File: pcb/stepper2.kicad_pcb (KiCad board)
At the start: 2 copper layers, 92 x 138 mm, 58 parts, among them J1 DA15_Receptacle_MountingHoles, J10 Conn_01x07_Pin, J11 FAN, J12 Conn_01x03_Pin, J13 Conn_01x03_Pin, J14 Conn_01x03_Pin, J2 DA15_Receptacle_MountingHoles, J3 DA15_Receptacle_MountingHoles, J4 DE15_Receptacle_HighDensity, J5 DE15_Receptacle_HighDensity, J6 DE15_Receptacle_HighDensity, J7 Conn_01x04_Pin, J8 Conn_01x05_Pin, J9 Conn_01x06_Pin, SW1 SW_Push, SW2 SW_Push, SW3 SW_Push, SW4 SW_Push, SW5 SW_Push, SW6 SW_Push, U1 AM26LS32ACN, U2 AM26LS32Ax, U3 AM26LS32ACN, U4 TMC2209_BIGTREETECH, U5 TMC2209_BIGTREETECH, U6 TMC2209_BIGTREETECH

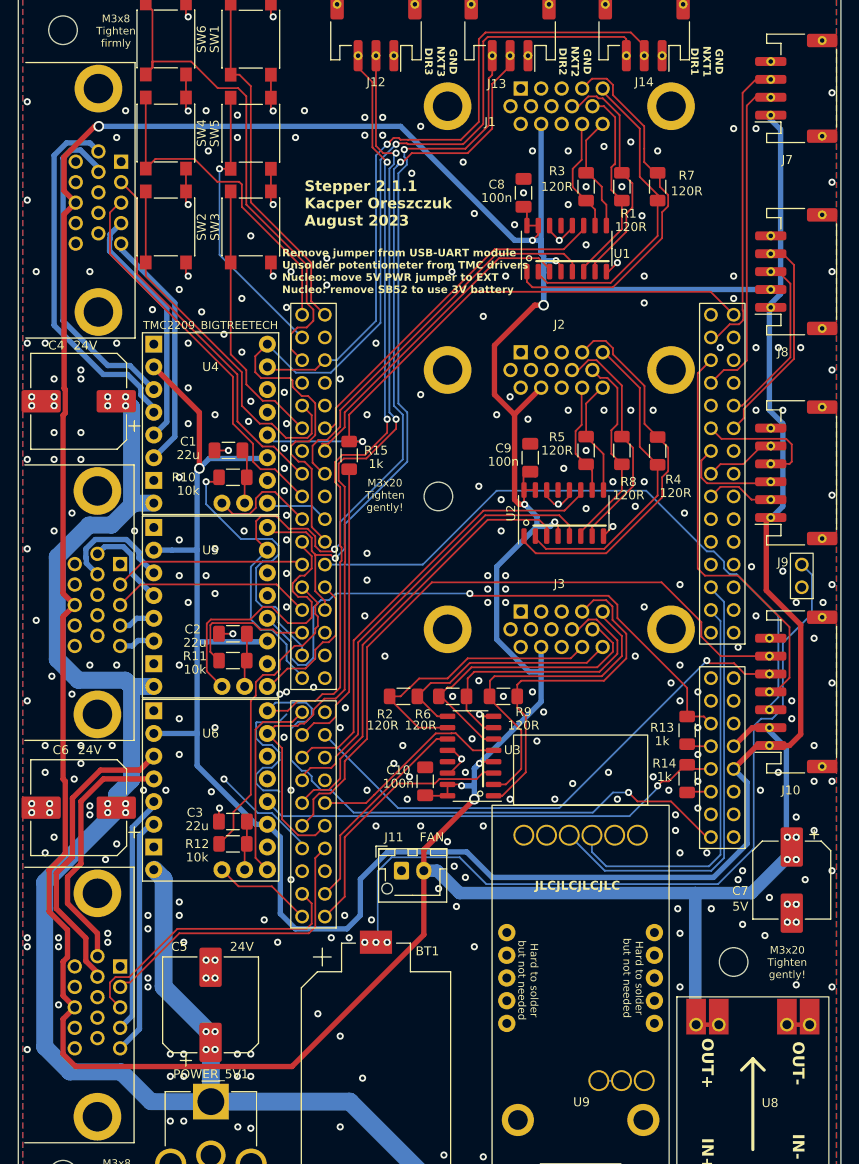
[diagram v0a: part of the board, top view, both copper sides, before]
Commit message: fixed flipped rotation direction relative to stepper 1
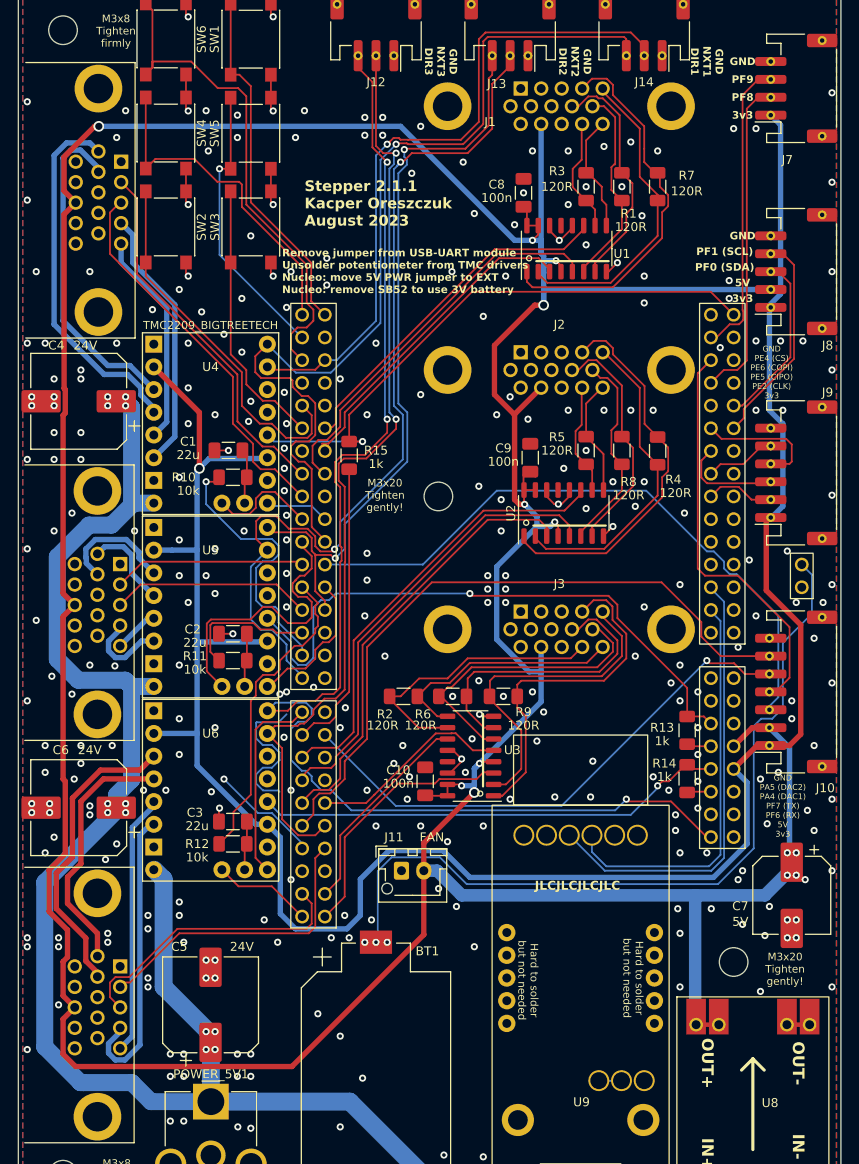
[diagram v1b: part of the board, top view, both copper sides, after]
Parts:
- moved C7 1.70 mm to (86.5, 101.8)
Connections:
- J4 pad 4: MYA1 -> MYB1
- J4 pad 5: MYB1 -> MYA1
- J5 pad 4: MYA2 -> MYB2
- J5 pad 5: MYB2 -> MYA2
- J6 pad 4: MYA3 -> MYB3
- J6 pad 5: MYB3 -> MYA3
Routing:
- net MYB3: track 26.8 -> 33.4 mm
- net MYB2: track 3.96 -> 9.51 mm
- net +5V: track 467.5 -> 472.3 mm
- net MYA1: track 27.5 -> 24.1 mm
- net MYB1: track 27.4 -> 29.7 mm
- net MYA3: track 26.9 -> 29.2 mm
- net MYA2: track 4.10 -> 5.04 mm
- net DIR3: track 151.2 -> 150.4 mm
- net GND: vias 333 -> 330
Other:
- board text added: "3v3"
- board text added: "5V"
- board text added: "GND"
- board text added: "GND PA5 (DAC2) PA4 (DAC1) PF7 (TX) PF6 (RX) 5V 3v3"
- board text added: "GND PE4 (CS) PE6 (COPI) PE5 (CIPO) PE2 (CLK) 3v3"
- board text added: "PF0 (SDA)"
- board text added: "PF1 (SCL)"
- board text added: "PF8"
- board text added: "PF9"

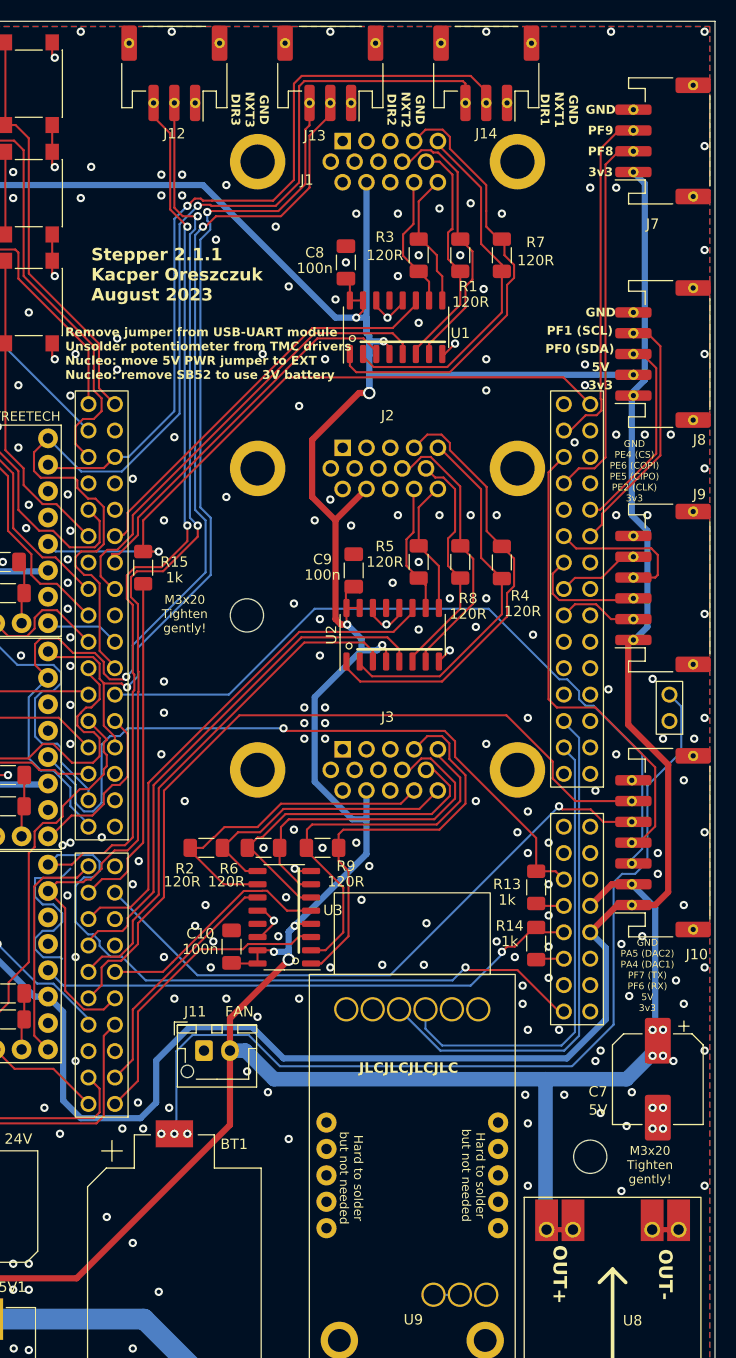
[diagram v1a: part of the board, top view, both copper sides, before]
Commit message: Added voltage shifter between FTDI and board
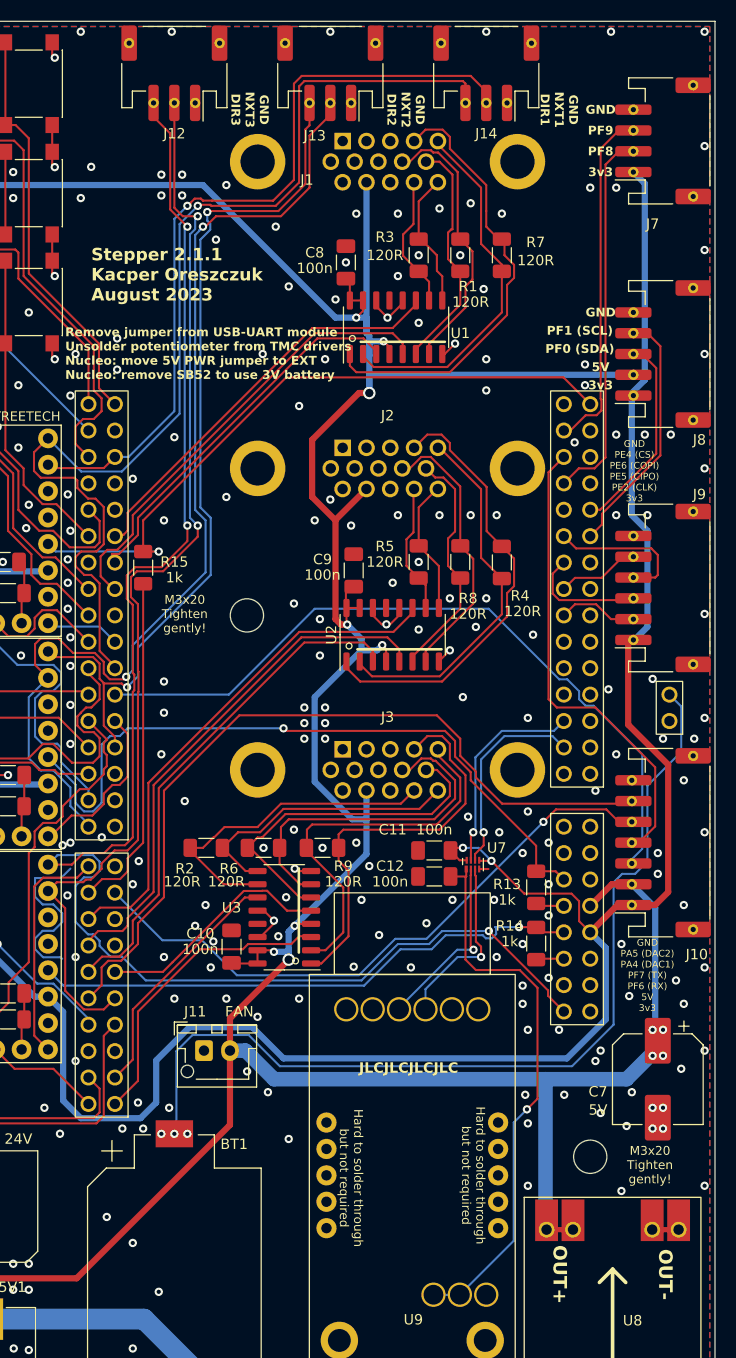
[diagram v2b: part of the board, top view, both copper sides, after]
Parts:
- added C11: 100n, Capacitor_SMD:C_1206_3216Metric_Pad1.33x1.80mm_HandSolder, F.Cu at (65.0, 79.8)
- added C12: 100n, Capacitor_SMD:C_1206_3216Metric_Pad1.33x1.80mm_HandSolder, F.Cu at (65.0, 82.2)
- added U7: ~, Package_DFN_QFN:OnSemi_UDFN-8_1.2x1.8mm_P0.4mm, F.Cu at (68.7, 81.1)
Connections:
- net Net-(U9-3V3) renamed FTDI_VCCIO
- U9 pad 3: USBUARTRX -> FTDI_TX
- U9 pad 4: USBUARTTX -> FTDI_RX
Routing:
- net FTDI_VCCIO: track 2.54 -> 53.5 mm, vias 0 -> 1
- net USBUARTTX: track 50.7 -> 20.0 mm, vias 0 -> 1
- net USBUARTRX: track 45.5 -> 19.5 mm, vias 0 -> 1
- net +3V3: track 246.8 -> 267.8 mm, vias 1 -> 3
- net FTDI_RX: track 0.00 -> 17.5 mm, vias 0 -> 1
- net FTDI_TX: track 0.00 -> 17.3 mm, vias 0 -> 1
- net DIR3: track 150.4 -> 153.6 mm
- net +5V: track 472.3 -> 471.4 mm
- net GND: track 72.7 -> 73.6 mm
- net TMCUART3: track 52.9 -> 53.5 mm
- net EXTDAC2: track 75.8 -> 76.4 mm
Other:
- board text added: "Hard to solder through but not required"
- board text removed: "Hard to solder but not needed"

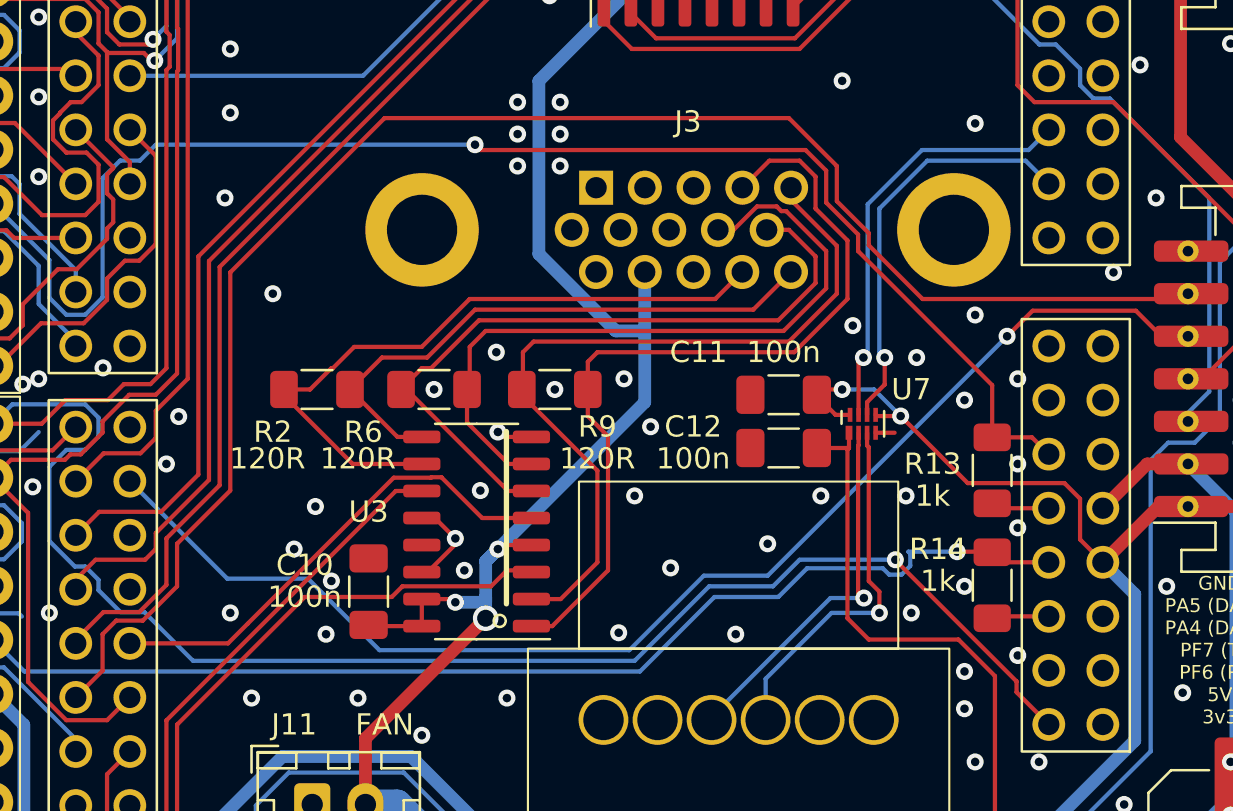
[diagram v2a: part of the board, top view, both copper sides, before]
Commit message: universal footprint for UART level shifter
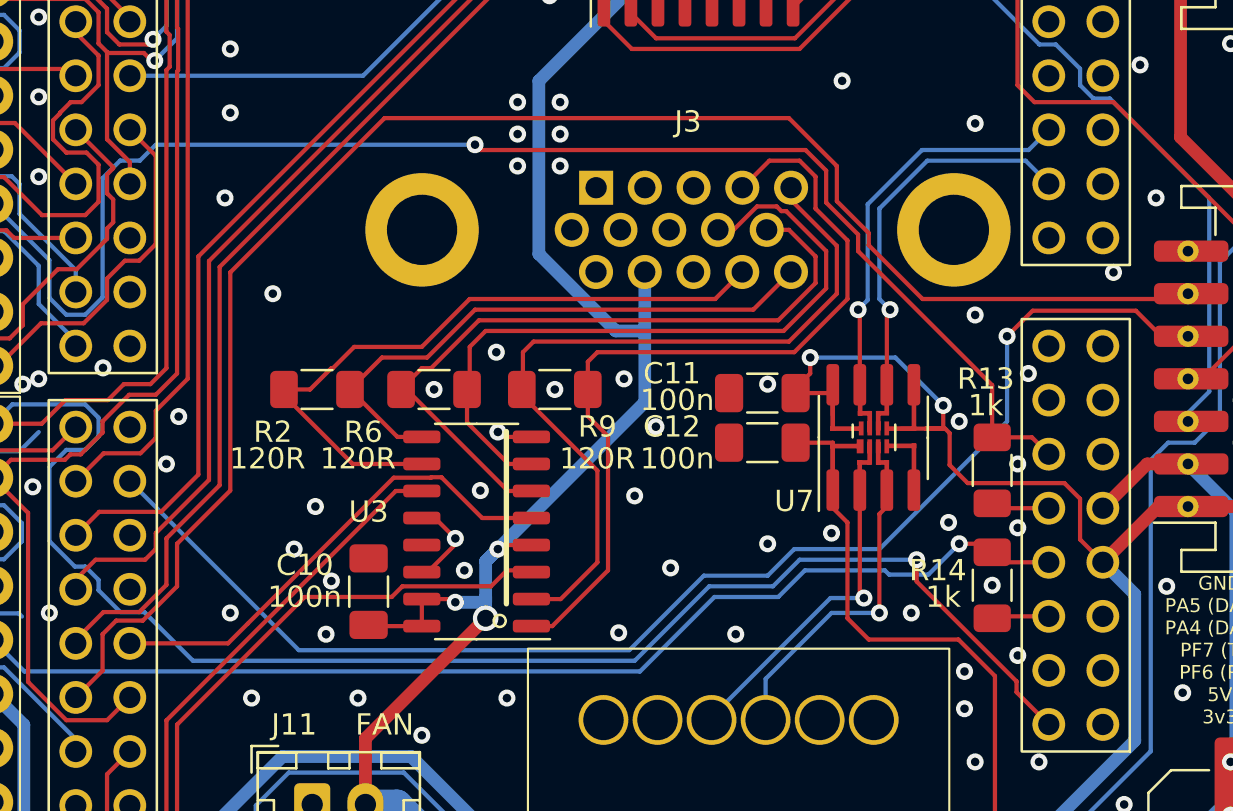
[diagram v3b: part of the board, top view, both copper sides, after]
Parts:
- U7: footprint Package_DFN_QFN:OnSemi_UDFN-8_1.2x1.8mm_P0.4mm -> stepper2:UDFN-8_1.2x1.8mm_OR_SO8_3.9x4.9mm
- moved C12 1.03 mm to (64.0, 82.0)
- moved C11 1.00 mm to (64.0, 79.7)
- moved U7 0.80 mm to (69.2, 81.8), turned to 0 degrees
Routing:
- net +3V3: track 267.8 -> 274.7 mm
- net FTDI_TX: track 17.3 -> 14.5 mm
- net FTDI_RX: track 17.5 -> 14.8 mm
- net EXTDAC1: track 59.7 -> 62.1 mm
- net USBUARTRX: track 19.5 -> 17.9 mm
- net USBUARTTX: track 20.0 -> 18.7 mm
- net GND: track 73.6 -> 72.7 mm, vias 330 -> 329
- net DIR3: track 153.6 -> 154.2 mm

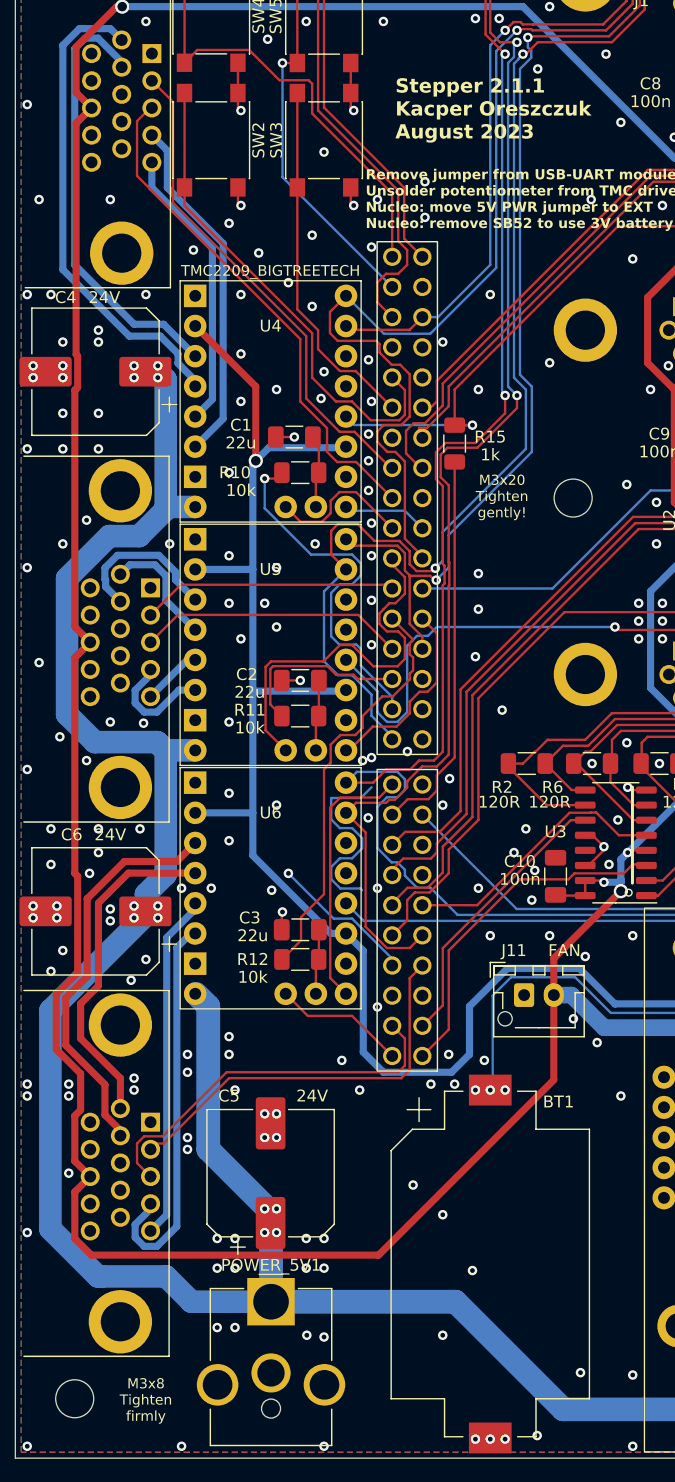
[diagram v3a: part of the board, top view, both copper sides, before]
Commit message: minor fixes and optimizations for PCB and bottom case part
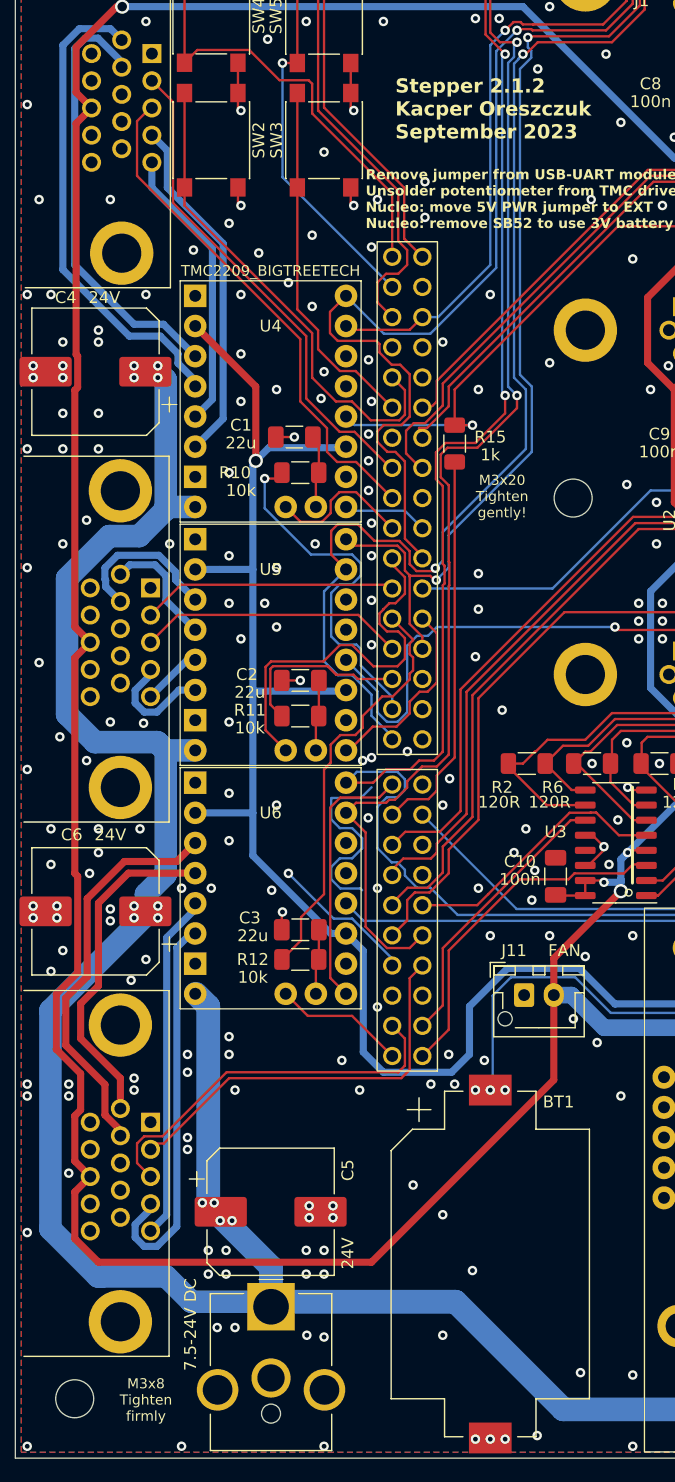
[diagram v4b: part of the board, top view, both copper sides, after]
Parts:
- 7.5-24V DC: renamed from POWER_5V1
- moved C5 3.25 mm to (21.5, 117.2), turned to 0 degrees
- moved 7.5-24V DC 0.42 mm to (21.5, 125.2)
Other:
- board text added: "Stepper 2.1.2 Kacper Oreszczuk September 2023"
- board text removed: "Stepper 2.1.1 Kacper Oreszczuk August 2023"

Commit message: top part of the case, adjustments to the PCB
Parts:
- J4, J5, J6: moved to B.Cu
- moved SW2 141.5 mm to (16.8, -114.5), turned to -90 degrees
- moved SW3 141.5 mm to (25.8, -114.5), turned to 180 degrees
- moved SW5 140.0 mm to (25.8, -123.5), turned to -90 degrees
- moved SW4 140.0 mm to (16.8, -123.5), turned to 180 degrees
- moved J3 139.0 mm to (60.5, -67.0)
- moved SW1 138.5 mm to (25.8, -132.5), turned to 180 degrees
- moved SW6 138.5 mm to (16.8, -132.5), turned to -90 degrees
- moved C6 138.5 mm to (5.75, -46.5), turned to -90 degrees
- moved U9 138.4 mm to (62.9, -15.9)
- moved U3 138.2 mm to (50.6, -52.0)
- moved C4 138.0 mm to (5.75, -91.5), turned to 90 degrees
- moved 7.5-24V DC 138.0 mm to (21.5, -12.8)
- moved BT1 138.0 mm to (40.0, -16.4)
- moved C1 138.0 mm to (23.5, -86.0)
- moved C10 138.0 mm to (45.5, -49.0)
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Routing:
- net GND: track 72.7 -> 51.7 mm, vias 329 -> 326
- net VCC: track 204.2 -> 222.4 mm
- net MXB1: track 37.2 -> 28.1 mm
- net DOWN1: track 56.2 -> 49.3 mm
- net MXA3: track 28.5 -> 22.4 mm
- net MXB3: track 33.7 -> 28.4 mm
- net UP3: track 30.6 -> 35.8 mm
- net NXT1: track 76.2 -> 79.3 mm
- net DIR1: track 106.9 -> 110.0 mm
- net DIR2: track 85.0 -> 88.0 mm
- net NXT2: track 101.3 -> 103.5 mm
- net MXA1: track 40.8 -> 39.1 mm
- net USBUARTRX: track 17.9 -> 19.5 mm
- net ENCI3-: track 27.3 -> 28.8 mm
- net DOWN3: track 41.5 -> 43.0 mm
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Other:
- board text added: "M3x16"
- board text added: "M3x20"
- board text added: "M3x30"
- board text removed: "M3x20 Tighten gently!"
- board text removed: "M3x8 Tighten firmly"
